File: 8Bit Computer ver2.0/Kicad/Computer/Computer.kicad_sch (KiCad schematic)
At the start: 4 parts, among them IC182 SN74F521DWR, IC183 SN74F521DWR, IC184 SN74LVC1G14DBVR, IC185 SN74LVC1G14DBVR

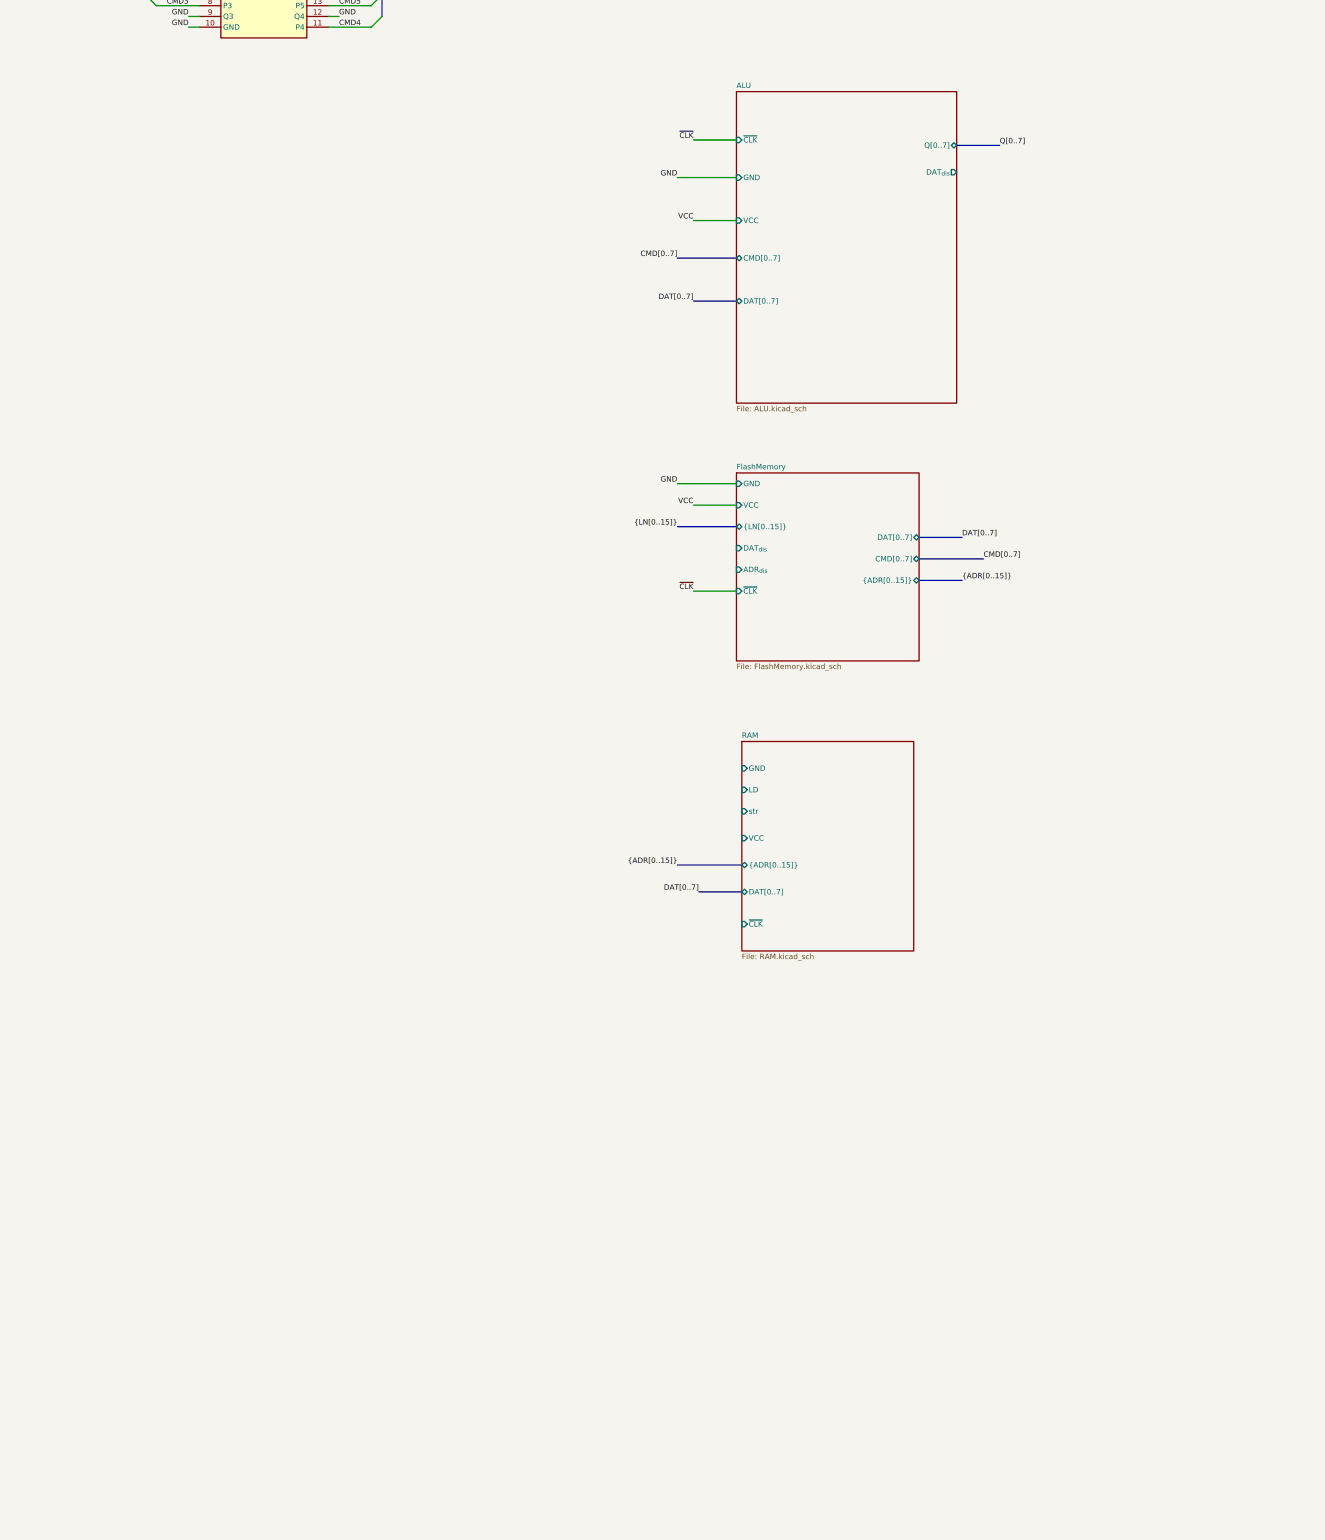
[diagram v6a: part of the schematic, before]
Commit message: Kicad
included Delay, pin Strips and headers, 8xnot
added some comps
finished flash mem
added DATtoADR
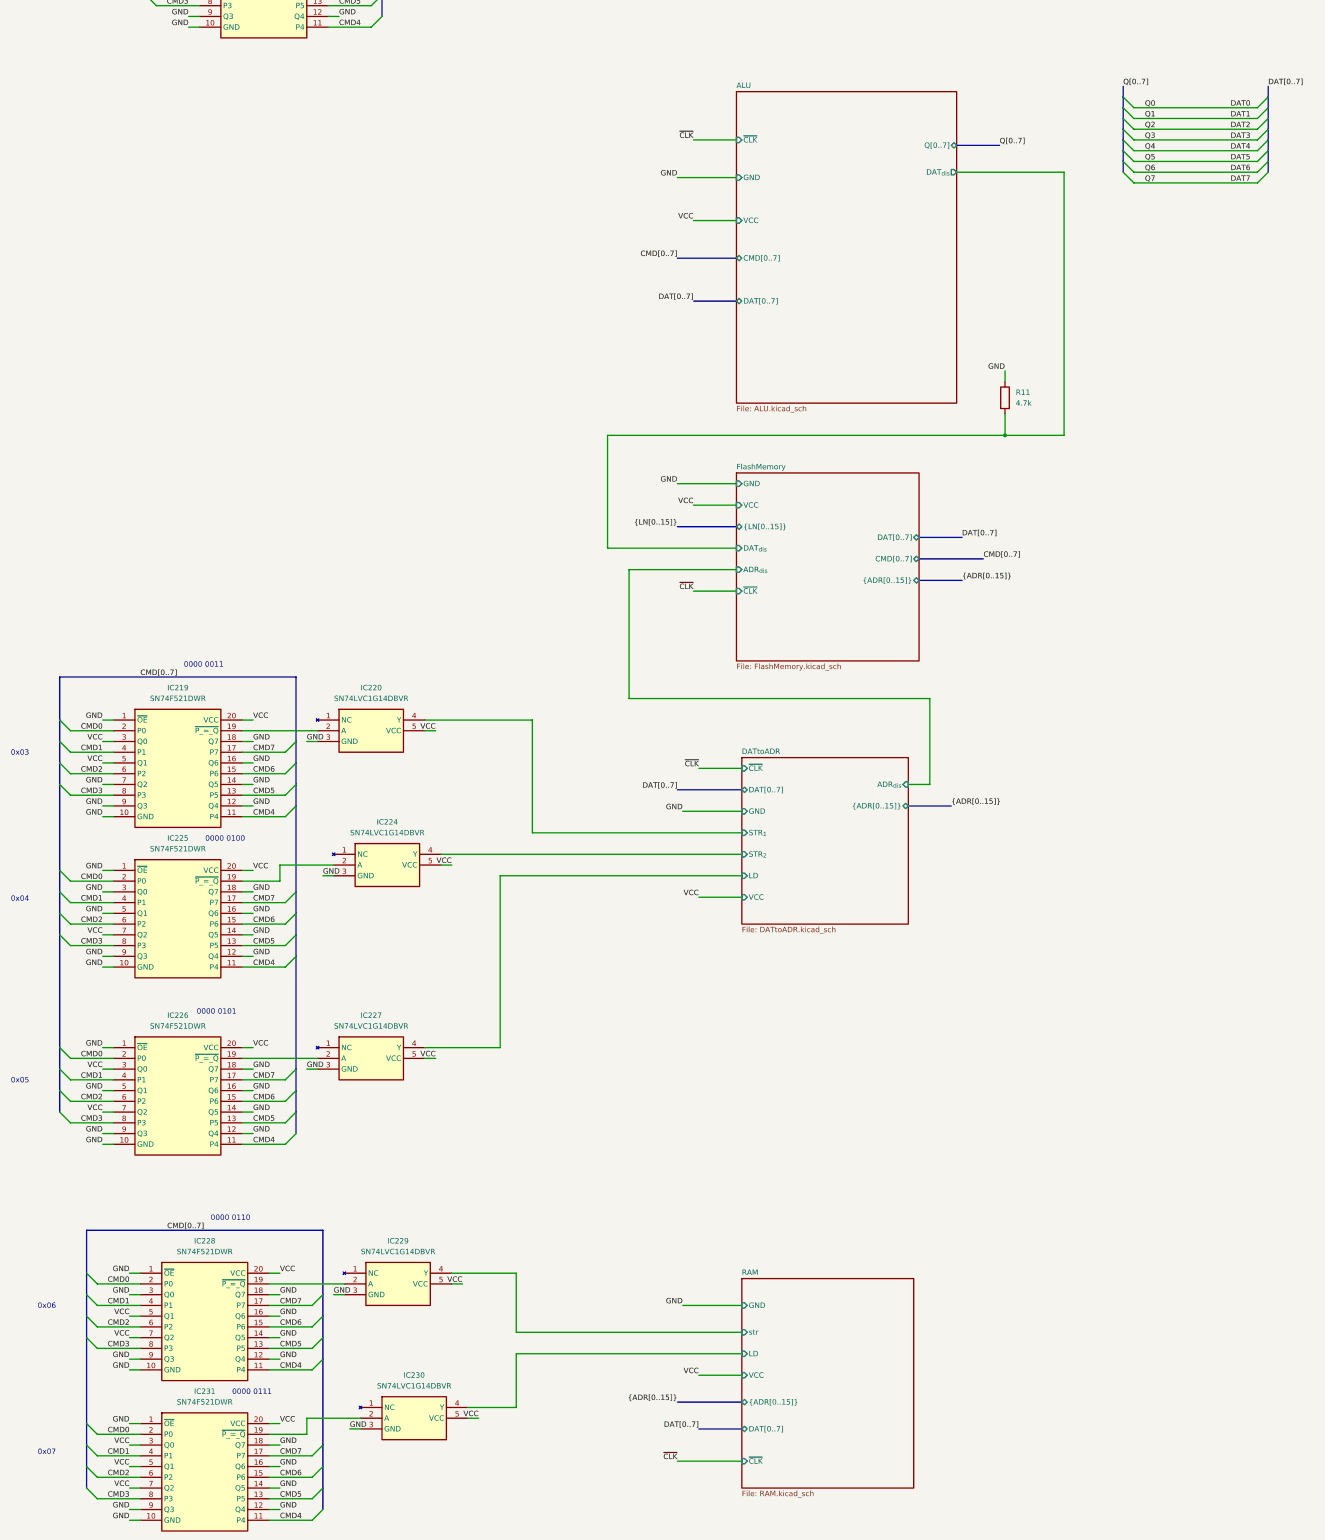
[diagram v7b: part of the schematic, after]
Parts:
- added IC219, IC225, IC226, IC228, IC231: SN74F521DWR, Samacsys:SOIC127P1030X265-20N, symbol Samacsys:SN74F521DWR
- added IC220, IC224, IC227, IC229, IC230: SN74LVC1G14DBVR, Samacsys:SOT95P280X145-5N, symbol Samacsys:SN74LVC1G14DBVR
- added R11: 4.7k, Resistor_SMD:R_1206_3216Metric_Pad1.30x1.75mm_HandSolder, symbol Device:R
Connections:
- net ALU/DAT_{dis}: now also R11.2
- net CMD0: now also IC219.2 (P0), IC225.2 (P0), IC226.2 (P0), IC228.2 (P0), IC231.2 (P0)
- net CMD1: now also IC219.4 (P1), IC225.4 (P1), IC226.4 (P1), IC228.4 (P1), IC231.4 (P1)
- net CMD2: now also IC219.6 (P2), IC225.6 (P2), IC226.6 (P2), IC228.6 (P2), IC231.6 (P2)
- net CMD3: now also IC219.8 (P3), IC225.8 (P3), IC226.8 (P3), IC228.8 (P3), IC231.8 (P3)
- net CMD4: now also IC219.11 (P4), IC225.11 (P4), IC226.11 (P4), IC228.11 (P4), IC231.11 (P4)
- net CMD5: now also IC219.13 (P5), IC225.13 (P5), IC226.13 (P5), IC228.13 (P5), IC231.13 (P5)
- net CMD6: now also IC219.15 (P6), IC225.15 (P6), IC226.15 (P6), IC228.15 (P6), IC231.15 (P6)
- net CMD7: now also IC219.17 (P7), IC225.17 (P7), IC226.17 (P7), IC228.17 (P7), IC231.17 (P7)
- net GND: now also IC219.1 (~{OE}), IC219.10 (GND), IC219.12 (Q4), IC219.14 (Q5), IC219.16 (Q6), IC219.18 (Q7), IC219.7 (Q2), IC219.9 (Q3), IC220.3 (GND), IC224.3 (GND), IC225.1 (~{OE}), IC225.10 (GND), IC225.12 (Q4), IC225.14 (Q5), IC225.16 (Q6), IC225.18 (Q7), IC225.3 (Q0), IC225.5 (Q1), IC225.9 (Q3), IC226.1 (~{OE}), IC226.10 (GND), IC226.12 (Q4), IC226.14 (Q5), IC226.16 (Q6), IC226.18 (Q7), IC226.5 (Q1), IC226.9 (Q3), IC227.3 (GND), IC228.1 (~{OE}), IC228.10 (GND), IC228.12 (Q4), IC228.14 (Q5), IC228.16 (Q6), IC228.18 (Q7), IC228.3 (Q0), IC228.9 (Q3), IC229.3 (GND), IC230.3 (GND), IC231.1 (~{OE}), IC231.10 (GND), IC231.12 (Q4), IC231.14 (Q5), IC231.16 (Q6), IC231.18 (Q7), IC231.9 (Q3), R11.1
- net RAM/LD: now also IC230.4 (Y)
- net RAM/str: now also IC229.4 (Y)
- net VCC: now also IC219.20 (VCC), IC219.3 (Q0), IC219.5 (Q1), IC220.5 (VCC), IC224.5 (VCC), IC225.20 (VCC), IC225.7 (Q2), IC226.20 (VCC), IC226.3 (Q0), IC226.7 (Q2), IC227.5 (VCC), IC228.20 (VCC), IC228.5 (Q1), IC228.7 (Q2), IC229.5 (VCC), IC230.5 (VCC), IC231.20 (VCC), IC231.3 (Q0), IC231.5 (Q1), IC231.7 (Q2)
- new net: IC219.19 (~{P_=_Q}), IC220.2 (A)
- new net: IC226.19 (~{P_=_Q}), IC227.2 (A)
- new net: IC230.2 (A), IC231.19 (~{P_=_Q})
- new net: IC228.19 (~{P_=_Q}), IC229.2 (A)
- new net: IC224.2 (A), IC225.19 (~{P_=_Q})
- new net DATtoADR/LD: IC227.4 (Y)
- new net DATtoADR/STR_{1}: IC220.4 (Y)
- new net DATtoADR/STR_{2}: IC224.4 (Y)
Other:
- added sheet DATtoADR (DATtoADR.kicad_sch)
- note added: "0000 0011"
- note added: "0000 0100"
- note added: "0000 0101"
- note added: "0000 0110"
- note added: "0000 0111"
- note added: "0x03"
- note added: "0x04"
- note added: "0x05"
- note added: "0x06"
- note added: "0x07"

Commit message: Kicad, parts
Parts:
added Leds
Kicad:
added Input Output
changed Q bus to DAT bus
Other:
- added sheet InputOutput (InputOutput.kicad_sch)
- sheet ALU ports: added none; removed Q[0..7]
- sheet DATtoADR ports: added none; removed ADR_{dis}
- moved on the sheet: IC182, IC183, IC184, IC185, IC219, IC220, IC224, IC225, IC226, IC227, IC228, IC229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
